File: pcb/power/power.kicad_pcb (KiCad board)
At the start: 2 copper layers, 36 parts, among them J1 Conn_Coaxial_Power, J2 GS3, SW1 SW_SPST, U1 L7805

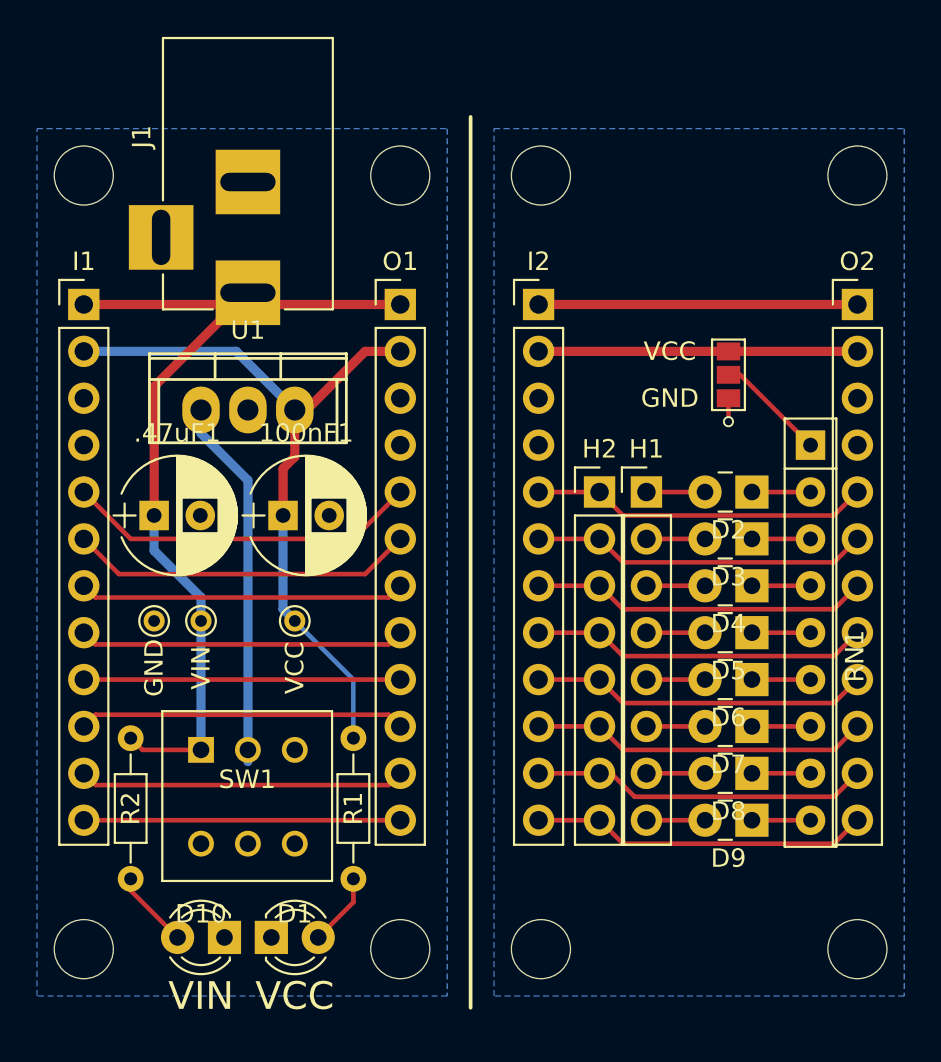
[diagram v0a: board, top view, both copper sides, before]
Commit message: Tidied up blank, and removed the voltage regulator from "power" module.
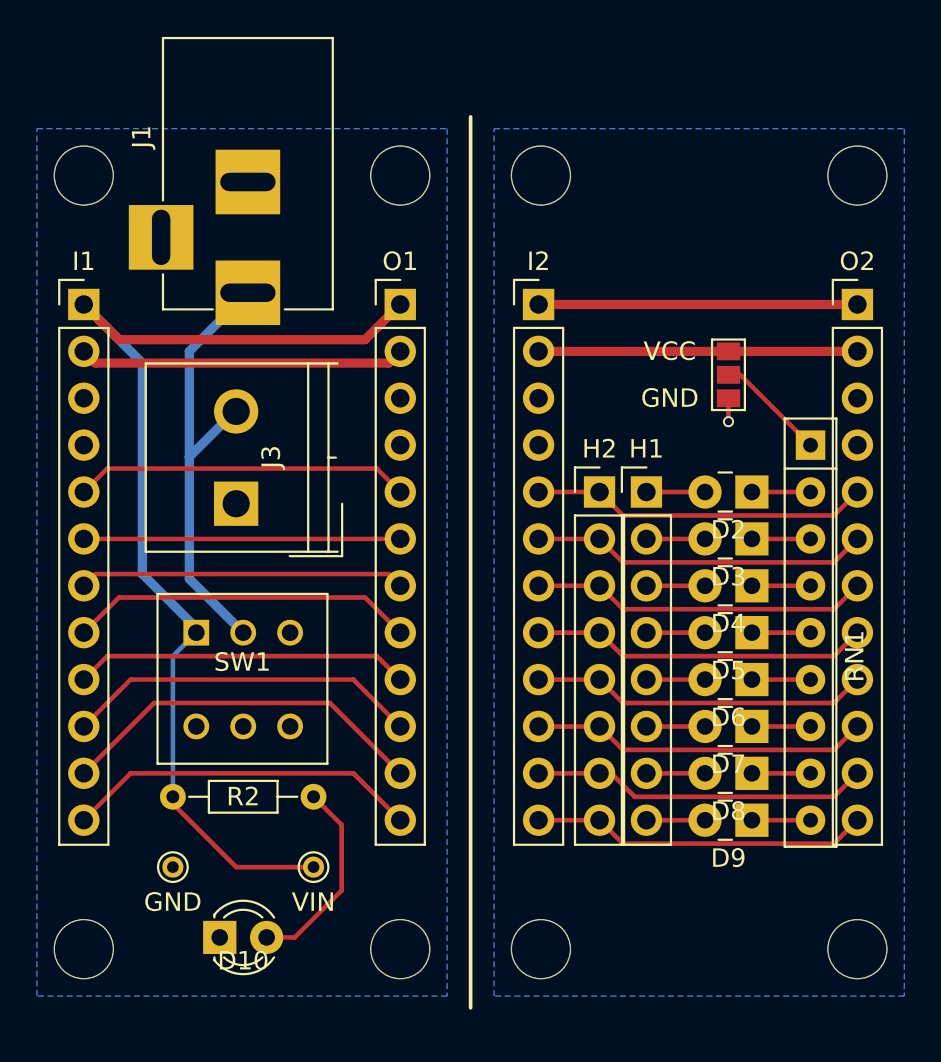
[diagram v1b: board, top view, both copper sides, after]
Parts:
- removed .47uF1, 100nF1: C, Capacitors_THT:CP_Radial_D6.3mm_P2.50mm
- removed D1: LED, LEDs:LED_D3.0mm
- removed R1: R, Resistors_THT:R_Axial_DIN0204_L3.6mm_D1.6mm_P7.62mm_Horizontal
- removed TP3: TEST, Connectors:PINTST
- removed U1: L7805, Power_Integrations:TO-220
- added J3: Screw_Terminal_01x02, Connectors_Terminal_Blocks:TerminalBlock_Philmore_TB132_02x5mm_Straight, F.Cu at (136.5, 104.1)
- moved TP1 14.7 mm to (140.7, 123.8)
- moved TP2 13.4 mm to (133.1, 123.8)
- moved SW1 6.36 mm to (134.4, 111.1)
- moved R2 3.91 mm to (133.1, 120.0), turned to 0 degrees
- moved D10 0.25 mm to (135.6, 127.6), turned to 0 degrees
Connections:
- J1 pad 1: /VIN -> /POWER
- SW1 pad 2: Net-(SW1-Pad2) -> /POWER
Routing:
- net /POWER: track 0.00 -> 24.5 mm
- net /VCC: track 39.4 -> 17.7 mm
- net Net-(SW1-Pad2): track 20.1 -> 0.00 mm
- net /VIN: track 46.6 -> 57.9 mm
- net Net-(D10-Pad2): track 4.23 -> 10.8 mm
- net Net-(D1-Pad2): track 3.96 -> 0.00 mm
- net /L6: track 17.7 -> 20.3 mm
- net /L7: track 17.1 -> 19.2 mm
- net /L1: track 18.7 -> 17.1 mm
- net /L5: track 17.7 -> 19.2 mm
- net /L4: track 17.1 -> 18.2 mm
- net /L0: track 19.2 -> 18.2 mm
- net /L3: track 17.7 -> 18.7 mm
